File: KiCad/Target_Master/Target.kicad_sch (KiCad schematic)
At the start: 0 parts

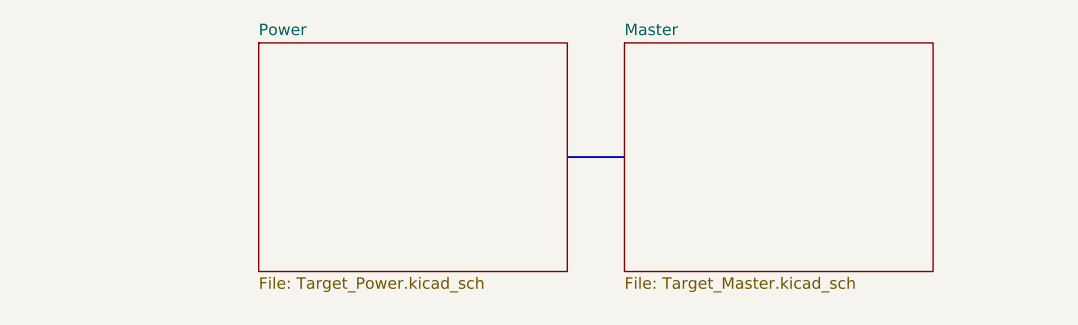
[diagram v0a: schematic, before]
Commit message: adding/fixing UART in master schematic.
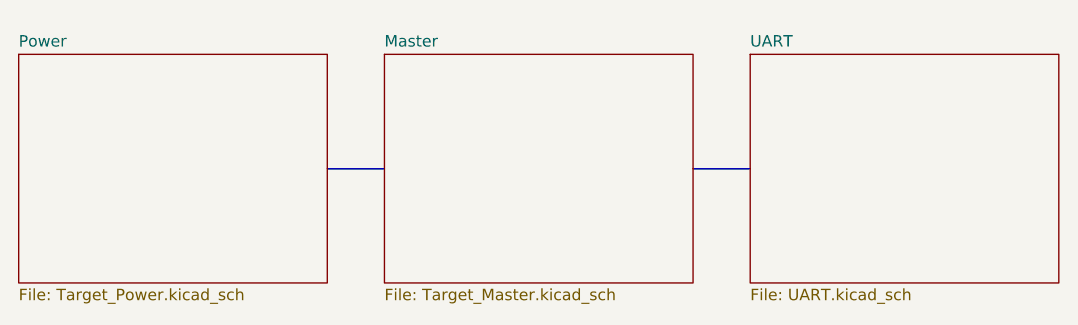
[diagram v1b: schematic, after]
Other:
- added sheet UART (UART.kicad_sch)
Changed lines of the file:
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@@
 	(title_block
 		(title "Laser Shooting Game Target Master")
-		(date "2024-12-06")
+		(date "2025-04-04")
 		(rev "A")
 		(company "Idaho State University")
 	)
 	(rectangle
-		(start 137.16 100.33)
-		(end 143.51 100.33)
+		(start 110.49 101.6)
+		(end 116.84 101.6)
+		(stroke
+			(width 0)
+			(type default)
+		)
+		(fill
+			(type none)
+		)
+	)
+	(rectangle
+		(start 151.13 101.6)
+		(end 157.48 101.6)
 		(stroke
 			(width 0)
@@
 	)
 	(sheet
-		(at 143.51 87.63)
+		(at 116.84 88.9)
 		(size 34.29 25.4)
 		(fields_autoplaced yes)
@@
 		)
 		(property "Sheetname" "Master"
-			(at 143.51 86.9184 0)
+			(at 116.84 88.1884 0)
 			(effects
 				(font
@@
 		)
 		(property "Sheetfile" "Target_Master.kicad_sch"
-			(at 143.51 113.6146 0)
+			(at 116.84 114.8846 0)
 			(effects
 				(font
@@
 	)
 	(sheet
-		(at 102.87 87.63)
+		(at 76.2 88.9)
 		(size 34.29 25.4)
 		(fields_autoplaced yes)
@@
 		)
 		(property "Sheetname" "Power"
-			(at 102.87 86.9184 0)
+			(at 76.2 88.1884 0)
 			(effects
 				(font
@@
 		)
 		(property "Sheetfile" "Target_Power.kicad_sch"
-			(at 102.87 113.6146 0)
+			(at 76.2 114.8846 0)
 			(effects
 				(font
@@
 				)
 			)
+		)
+	)
+	(sheet
+		(at 157.48 88.9)
+		(size 34.29 25.4)
+		(fields_autoplaced yes)
+		(stroke
+			(width 0.1524)
+			(type solid)
+		)
+		(fill
+			(color 0 0 0 0.0000)
+		)
+		(property "Sheetname" "UART"
+			(at 157.48 88.1884 0)
+			(effects
+				(font
+					(size 1.27 1.27)
+				)
+				(justify left bottom)
+			)
+		)
+		(property "Sheetfile" "UART.kicad_sch"
+			(at 157.48 114.8846 0)
+			(effects
+				(font
+					(size 1.27 1.27)
+				)
+				(justify left top)
+			)
+		)
+		(instances
+			(project "Target"
+				(path "/b95a4fbb-e866-40f1-8b06-3d5c3eea26d9"
+					(page "4")
+				)
+			)
